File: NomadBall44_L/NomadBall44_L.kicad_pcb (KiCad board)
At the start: 2 copper layers, 149 x 203 mm, 58 parts, among them SW1 SW_Push, SW10 SW_Push, SW11 SW_Push, SW12 SW_Push, SW13 SW_Push, SW14 SW_Push, SW15 SW_Push, SW16 SW_Push, SW17 SW_Push, SW18 SW_Push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

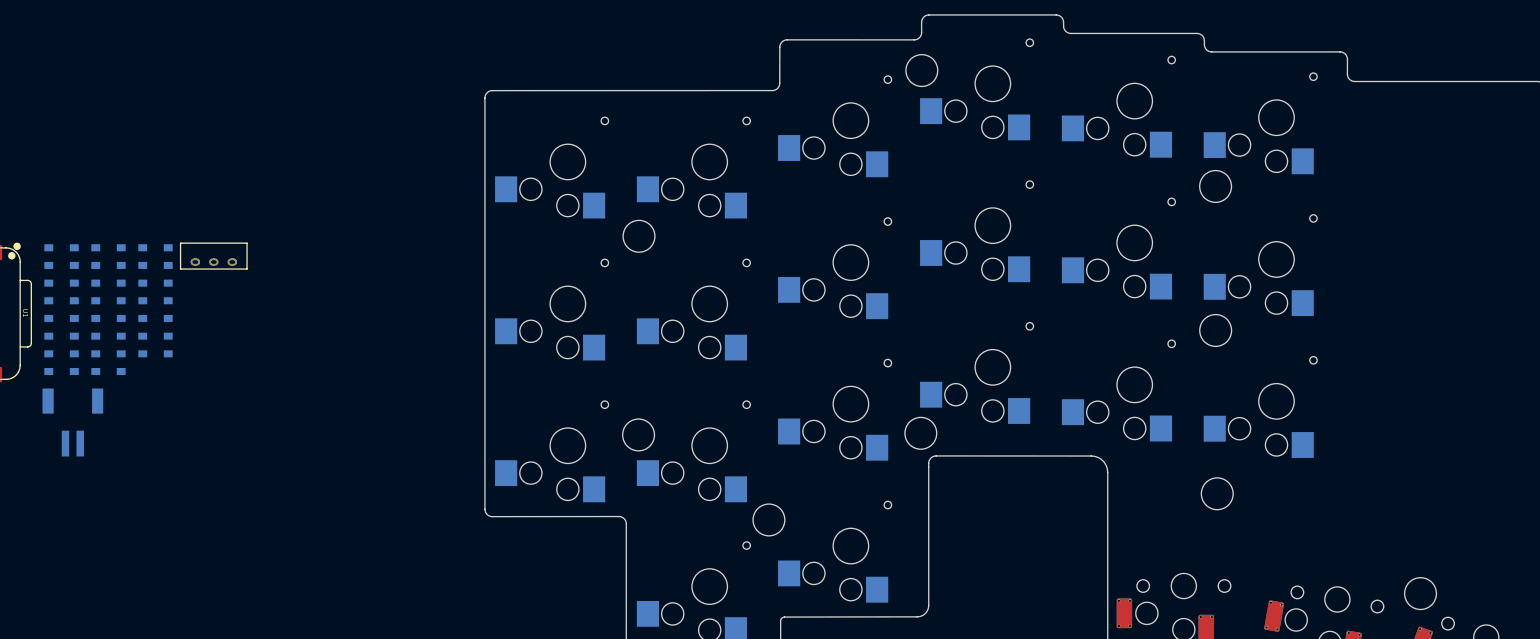
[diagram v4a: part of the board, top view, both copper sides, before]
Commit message: ダイオードを配置
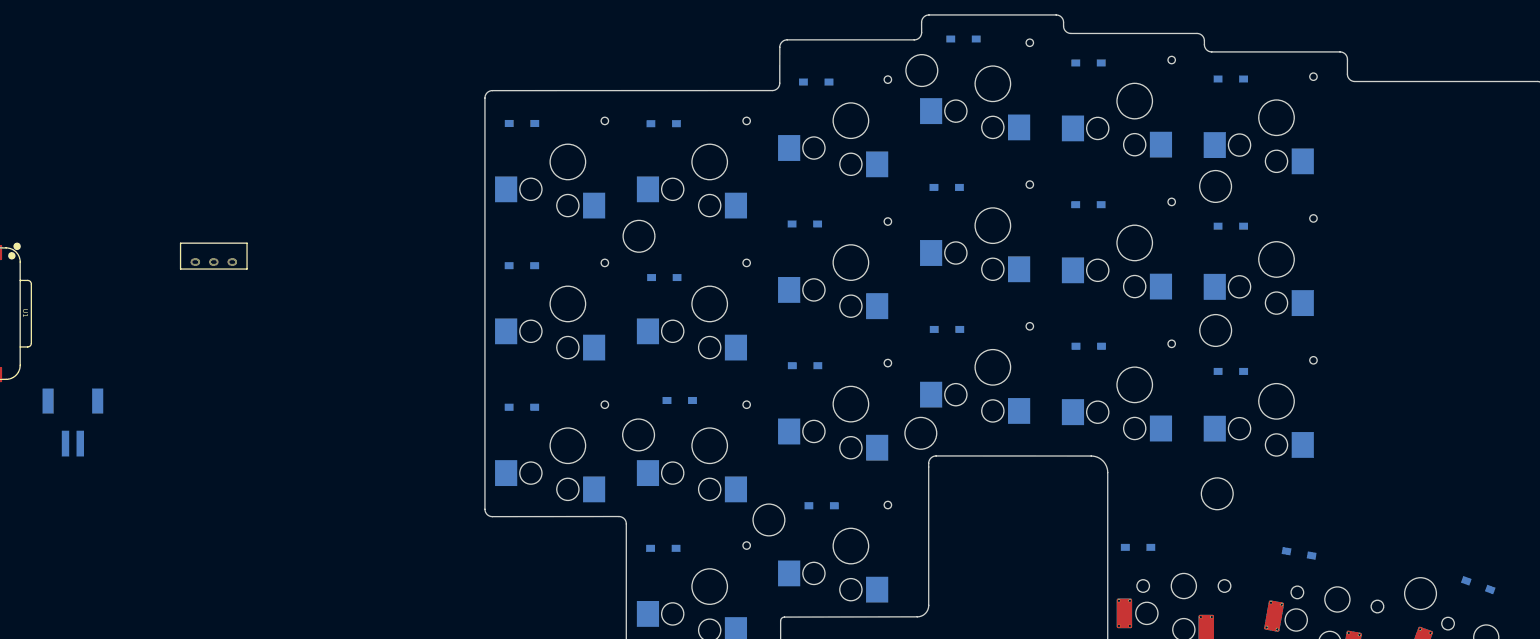
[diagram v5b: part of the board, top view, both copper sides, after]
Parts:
- moved D19 183.5 mm to (263.6, 131.3), turned to -20 degrees
- moved D1 159.8 mm to (230.0, 63.8)
- moved D7 159.1 mm to (230.0, 83.7)
- moved D20 158.4 mm to (239.3, 127.5), turned to -10 degrees
- moved D13 152.0 mm to (230.0, 103.4)
- moved D2 141.6 mm to (210.7, 61.6)
- moved D8 140.7 mm to (210.7, 80.8)
- moved D21 136.5 mm to (217.4, 127.2)
- moved D14 132.6 mm to (210.8, 100.0)
- moved D3 126.4 mm to (193.8, 58.4)
- moved D9 113.7 mm to (191.6, 78.5)
- moved D15 113.5 mm to (191.6, 97.7)
- moved D4 106.3 mm to (173.9, 64.2)
- moved D10 94.4 mm to (172.4, 83.4)
- moved D16 94.2 mm to (172.4, 102.6)
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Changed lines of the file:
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@@
 	(footprint "NomadBall44:Diode_SMD"
 		(layer "F.Cu")
-		(at 71.8365 93.813698)
+		(at 173.916875 64.23)
 		(descr "https://github.com/e3w2q/su120-keyboard (diode_SMD_rev2)")
 		(property "Reference" "D4"
@@
 	(footprint "NomadBall44:Diode_SMD"
 		(layer "F.Cu")
-		(at 84.54275 89.032442)
+		(at 134.106875 108.21)
 		(descr "https://github.com/e3w2q/su120-keyboard (diode_SMD_rev2)")
 		(property "Reference" "D18"
@@
 	(footprint "NomadBall44:Diode_SMD"
 		(layer "F.Cu")
-		(at 84.54275 98.594954)
+		(at 174.646875 121.54)
 		(descr "https://github.com/e3w2q/su120-keyboard (diode_SMD_rev2)")
 		(property "Reference" "D22"
@@
 	(footprint "NomadBall44:Diode_SMD"
 		(layer "F.Cu")
-		(at 78.189625 86.641814)
+		(at 191.566875 78.48)
 		(descr "https://github.com/e3w2q/su120-keyboard (diode_SMD_rev2)")
 		(property "Reference" "D9"
@@
 	(footprint "NomadBall44:Diode_SMD"
 		(layer "F.Cu")
-		(at 84.54275 96.204326)
+		(at 217.446875 127.17)
 		(descr "https://github.com/e3w2q/su120-keyboard (diode_SMD_rev2)")
 		(property "Reference" "D21"
@@
 	(footprint "NomadBall44:Diode_SMD"
 		(layer "F.Cu")
-		(at 71.8365 98.594954)
+		(at 134.116875 69.83)
 		(descr "https://github.com/e3w2q/su120-keyboard (diode_SMD_rev2)")
 		(property "Reference" "D6"
@@
 	(footprint "NomadBall44:Diode_SMD"
 		(layer "F.Cu")
-		(at 71.8365 89.032442)
+		(at 210.746875 61.64)
 		(descr "https://github.com/e3w2q/su120-keyboard (diode_SMD_rev2)")
 		(property "Reference" "D2"
@@
 	(footprint "NomadBall44:Diode_SMD"
 		(layer "F.Cu")
-		(at 84.54275 93.813698)
+		(at 239.276875 127.5 -10)
 		(descr "https://github.com/e3w2q/su120-keyboard (diode_SMD_rev2)")
 		(property "Reference" "D20"
-			(at 3 -1 0)
+			(at 3 -1 170)
 			(layer "B.SilkS")
 			(effects
@@
 		)
 		(property "Value" "D"
-			(at 3.2 -1.6 0)
+			(at 3.2 -1.6 170)
 			(layer "F.Fab")
 			(hide yes)
@@
 		)
 		(property "Datasheet" "~"
-			(at 0 0 0)
+			(at 0 0 350)
 			(unlocked yes)
 			(layer "F.Fab")
@@
 		)
 		(property "Description" "Diode"
-			(at 0 0 0)
+			(at 0 0 350)
 			(unlocked yes)
 			(layer "F.Fab")
@@
 		)
 		(property "Sim.Device" "D"
-			(at 0 0 0)
+			(at 0 0 350)
 			(unlocked yes)
 			(layer "F.Fab")
@@
 		)
 		(property "Sim.Pins" "1=K 2=A"
-			(at 0 0 0)
+			(at 0 0 350)
 			(unlocked yes)
 			(layer "F.Fab")
@@
 		(attr smd)
 		(fp_line
-			(start 1.785943 0)
+			(start 1.785944 0)
 			(end 1.984381 0)
 			(stroke
@@
 		)
 		(fp_line
-			(start 1.984381 -0.595314)
-			(end 1.984381 0.595314)
+			(start 1.984381 0.595314)
+			(end 3.571885 0.595314)
 			(stroke
 				(width 0.2)
@@
 		)
 		(fp_line
-			(start 1.984381 0.595314)
-			(end 3.571885 0.595314)
+			(start 1.984381 -0.595314)
+			(end 1.984381 0.595314)
 			(stroke
 				(width 0.2)
@@
 		)
 		(fp_line
-			(start 3.571885 -0.595314)
-			(end 1.984381 -0.595314)
+			(start 3.571885 0.595314)
+			(end 3.571885 -0.595314)
 			(stroke
 				(width 0.2)
@@
 		)
 		(fp_line
-			(start 3.571885 0.595314)
-			(end 3.571885 -0.595314)
+			(start 3.571885 -0.595314)
+			(end 1.984381 -0.595314)
 			(stroke
 				(width 0.2)
@@
 		)
 		(pad "1" smd rect
-			(at 1.053125 0)
+			(at 1.053125 0 350)
 			(size 1.2 0.95)
 			(layers "B.Cu" "B.Mask" "B.Paste")
@@
 		)
 		(pad "2" smd rect
-			(at 4.503125 0)
+			(at 4.503125 0 350)
 			(size 1.2 0.95)
 			(layers "B.Cu" "B.Mask" "B.Paste")
@@
 	(footprint "NomadBall44:Diode_SMD"
 		(layer "F.Cu")
-		(at 71.8365 86.641814)
+		(at 229.993438 63.81)
 		(descr "https://github.com/e3w2q/su120-keyboard (diode_SMD_rev2)")
 		(property "Reference" "D1"
@@
 	(footprint "NomadBall44:Diode_SMD"
 		(layer "F.Cu")
-		(at 78.189625 98.594954)
+		(at 210.776875 99.96)
 		(descr "https://github.com/e3w2q/su120-keyboard (diode_SMD_rev2)")
 		(property "Reference" "D14"
@@
 	(footprint "NomadBall44:Diode_SMD"
 		(layer "F.Cu")
-		(at 71.8365 91.42307)
+		(at 193.836875 58.41)
 		(descr "https://github.com/e3w2q/su120-keyboard (diode_SMD_rev2)")
 		(property "Reference" "D3"
@@
 	(footprint "NomadBall44:Diode_SMD"
 		(layer "F.Cu")
-		(at 78.189625 100.985582)
+		(at 191.606875 97.69)
 		(descr "https://github.com/e3w2q/su120-keyboard (diode_SMD_rev2)")
 		(property "Reference" "D15"
@@
 	(footprint "NomadBall44:Diode_SMD"
 		(layer "F.Cu")
-		(at 84.54275 91.42307)
+		(at 263.636875 131.33 -20)
 		(descr "https://github.com/e3w2q/su120-keyboard (diode_SMD_rev2)")
 		(property "Reference" "D19"
-			(at 3 -1 0)
+			(at 3 -1 160)
 			(layer "B.SilkS")
 			(effects
@@
 		)
 		(property "Value" "D"
-			(at 3.2 -1.6 0)
+			(at 3.200001 -1.599999 160)
 			(layer "F.Fab")
 			(hide yes)
@@
 		)
 		(property "Datasheet" "~"
-			(at 0 0 0)
+			(at 0 0 340)
 			(unlocked yes)
 			(layer "F.Fab")
@@
 		)
 		(property "Description" "Diode"
-			(at 0 0 0)
+			(at 0 0 340)
 			(unlocked yes)
 			(layer "F.Fab")
@@
 		)
 		(property "Sim.Device" "D"
-			(at 0 0 0)
+			(at 0 0 340)
 			(unlocked yes)
 			(layer "F.Fab")
@@
 		)
 		(property "Sim.Pins" "1=K 2=A"
-			(at 0 0 0)
+			(at 0 0 340)
 			(unlocked yes)
 			(layer "F.Fab")
@@
 		(attr smd)
 		(fp_line
-			(start 1.785943 0)
-			(end 1.984381 0)
+			(start 1.984381 0.595314)
+			(end 3.571885 0.595314)
 			(stroke
 				(width 0.2)
@@
 		)
 		(fp_line
-			(start 1.984381 -0.595314)
-			(end 1.984381 0.595314)
+			(start 1.785944 0)
+			(end 1.984381 0)
 			(stroke
 				(width 0.2)
@@
 		)
 		(fp_line
-			(start 1.984381 0.595314)
-			(end 3.571885 0.595314)
+			(start 2.381257 0.595314)
+			(end 2.381257 -0.595314)
 			(stroke
 				(width 0.2)
@@
 		)
 		(fp_line
-			(start 2.381257 0.595314)
-			(end 2.381257 -0.595314)
+			(start 1.984381 -0.595314)
+			(end 1.984381 0.595314)
 			(stroke
 				(width 0.2)
@@
 		)
 		(fp_line
-			(start 3.571885 -0.595314)
-			(end 1.984381 -0.595314)
+			(start 3.571885 0.595314)
+			(end 3.571885 -0.595314)
 			(stroke
 				(width 0.2)
@@
 		)
 		(fp_line
-			(start 3.571885 0)
-			(end 3.770323 0)
+			(start 3.571885 -0.000001)
+			(end 3.770323 0.000001)
 			(stroke
 				(width 0.2)
@@
 		)
 		(fp_line
-			(start 3.571885 0.595314)
-			(end 3.571885 -0.595314)
+			(start 3.571885 -0.595314)
+			(end 1.984381 -0.595314)
 			(stroke
 				(width 0.2)
@@
 		)
 		(pad "1" smd rect
-			(at 1.053125 0)
+			(at 1.053125 0 340)
 			(size 1.2 0.95)
 			(layers "B.Cu" "B.Mask" "B.Paste")
@@
 		)
 		(pad "2" smd rect
-			(at 4.503125 0)
+			(at 4.503125 0 340)
 			(size 1.2 0.95)
 			(layers "B.Cu" "B.Mask" "B.Paste")
@@
 	(footprint "NomadBall44:Diode_SMD"
 		(layer "F.Cu")
-		(at 71.8365 100.985582)
+		(at 229.993438 83.72)
 		(descr "https://github.com/e3w2q/su120-keyboard (diode_SMD_rev2)")
 		(property "Reference" "D7"
@@
 	(footprint "NomadBall44:Diode_SMD"
 		(layer "F.Cu")
-		(at 84.54275 86.641814)
+		(at 155.456875 107.3)
 		(descr "https://github.com/e3w2q/su120-keyboard (diode_SMD_rev2)")
 		(property "Reference" "D17"
@@
 	(footprint "NomadBall44:Diode_SMD"
 		(layer "F.Cu")
-		(at 78.189625 93.813698)
+		(at 134.106875 89.06)
 		(descr "https://github.com/e3w2q/su120-keyboard (diode_SMD_rev2)")
 		(property "Reference" "D12"
@@
 	(footprint "NomadBall44:Diode_SMD"
 		(layer "F.Cu")
-		(at 78.189625 91.42307)
+		(at 153.366875 90.67)
 		(descr "https://github.com/e3w2q/su120-keyboard (diode_SMD_rev2)")
 		(property "Reference" "D11"
@@
 	(footprint "NomadBall44:Diode_SMD"
 		(layer "F.Cu")
-		(at 78.189625 103.37621)
+		(at 172.406875 102.59)
 		(descr "https://github.com/e3w2q/su120-keyboard (diode_SMD_rev2)")
 		(property "Reference" "D16"
@@
 	(footprint "NomadBall44:Diode_SMD"
 		(layer "F.Cu")
-		(at 84.54275 100.985582)
+		(at 153.236875 127.3)
 		(descr "https://github.com/e3w2q/su120-keyboard (diode_SMD_rev2)")
 		(property "Reference" "D23"
@@
 	(footprint "NomadBall44:Diode_SMD"
 		(layer "F.Cu")
-		(at 78.189625 96.204326)
+		(at 230.006875 103.37)
 		(descr "https://github.com/e3w2q/su120-keyboard (diode_SMD_rev2)")
 		(property "Reference" "D13"
@@
 	(footprint "NomadBall44:Diode_SMD"
 		(layer "F.Cu")
-		(at 71.8365 96.204326)
+		(at 153.286875 69.86)
 		(descr "https://github.com/e3w2q/su120-keyboard (diode_SMD_rev2)")
 		(property "Reference" "D5"
@@
 	(footprint "NomadBall44:Diode_SMD"
 		(layer "F.Cu")
-		(at 78.189625 89.032442)
+		(at 172.376875 83.42)
 		(descr "https://github.com/e3w2q/su120-keyboard (diode_SMD_rev2)")
 		(property "Reference" "D10"
@@
 	(footprint "NomadBall44:Diode_SMD"
 		(layer "F.Cu")
-		(at 71.8365 103.37621)
+		(at 210.736875 80.81)
 		(descr "https://github.com/e3w2q/su120-keyboard (diode_SMD_rev2)")
 		(property "Reference" "D8"

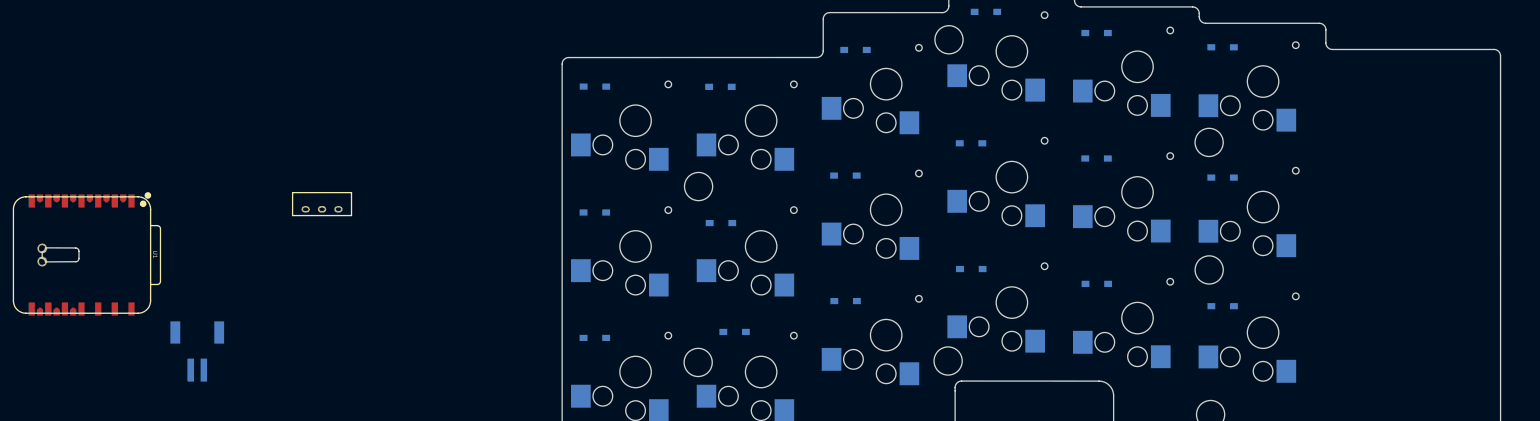
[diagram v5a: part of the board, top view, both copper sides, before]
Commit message: マイコン周りのフットプリントを配置
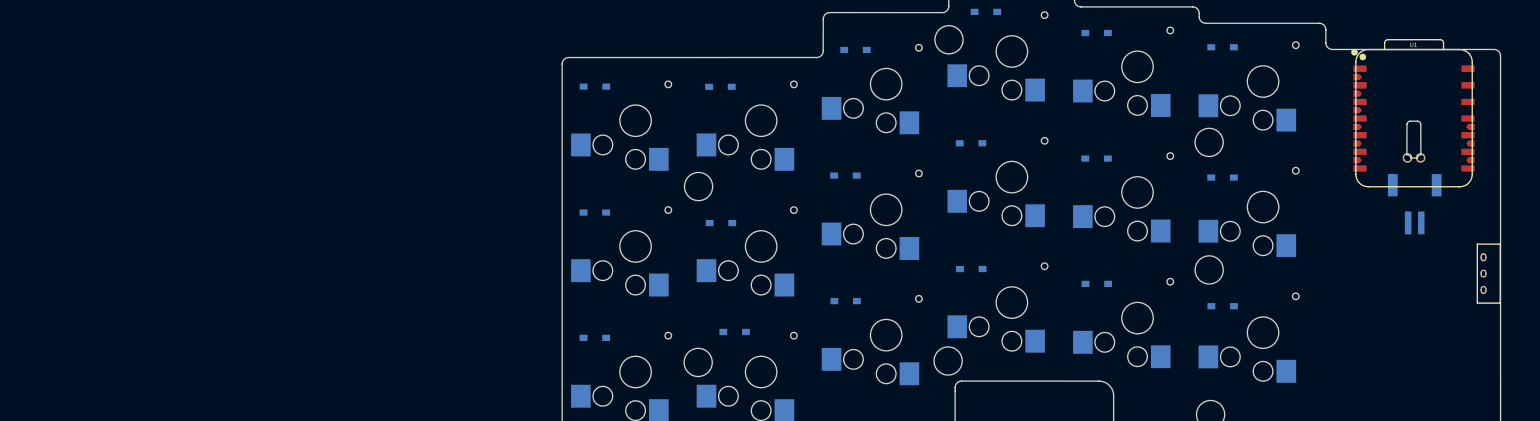
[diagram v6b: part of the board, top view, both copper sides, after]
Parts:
- moved U1 204.6 mm to (262.0, 74.7), turned to 90 degrees
- moved BT1 187.3 mm to (262.1, 90.6)
- moved SW24 178.8 mm to (273.7, 98.4), turned to -90 degrees

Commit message: マイコン周りの配線を実施
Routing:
- net Col5: track 0.00 -> 173.3 mm, vias 0 -> 9
- net Col2: track 0.00 -> 124.9 mm, vias 0 -> 7
- net Col1: track 0.00 -> 111.9 mm, vias 0 -> 11
- net Col4: track 0.00 -> 105.3 mm, vias 0 -> 1
- net Col3: track 0.00 -> 93.6 mm, vias 0 -> 3
- net Col0: track 0.00 -> 89.2 mm, vias 0 -> 9
- net Row1: track 0.00 -> 75.5 mm, vias 0 -> 7
- net Row2: track 0.00 -> 65.8 mm, vias 0 -> 5
- net Row0: track 0.00 -> 57.9 mm, vias 0 -> 5
- net Row3: track 0.00 -> 56.0 mm, vias 0 -> 3
- net GND: track 0.00 -> 47.4 mm, vias 0 -> 5
- net Net-(BT1--): track 0.00 -> 19.2 mm, vias 0 -> 1
- net Bat: track 0.00 -> 12.1 mm, vias 0 -> 1
